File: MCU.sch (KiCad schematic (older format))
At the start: 18 parts, among them J2 JTAG, J3 BOOT, U6 STM32F303RETx

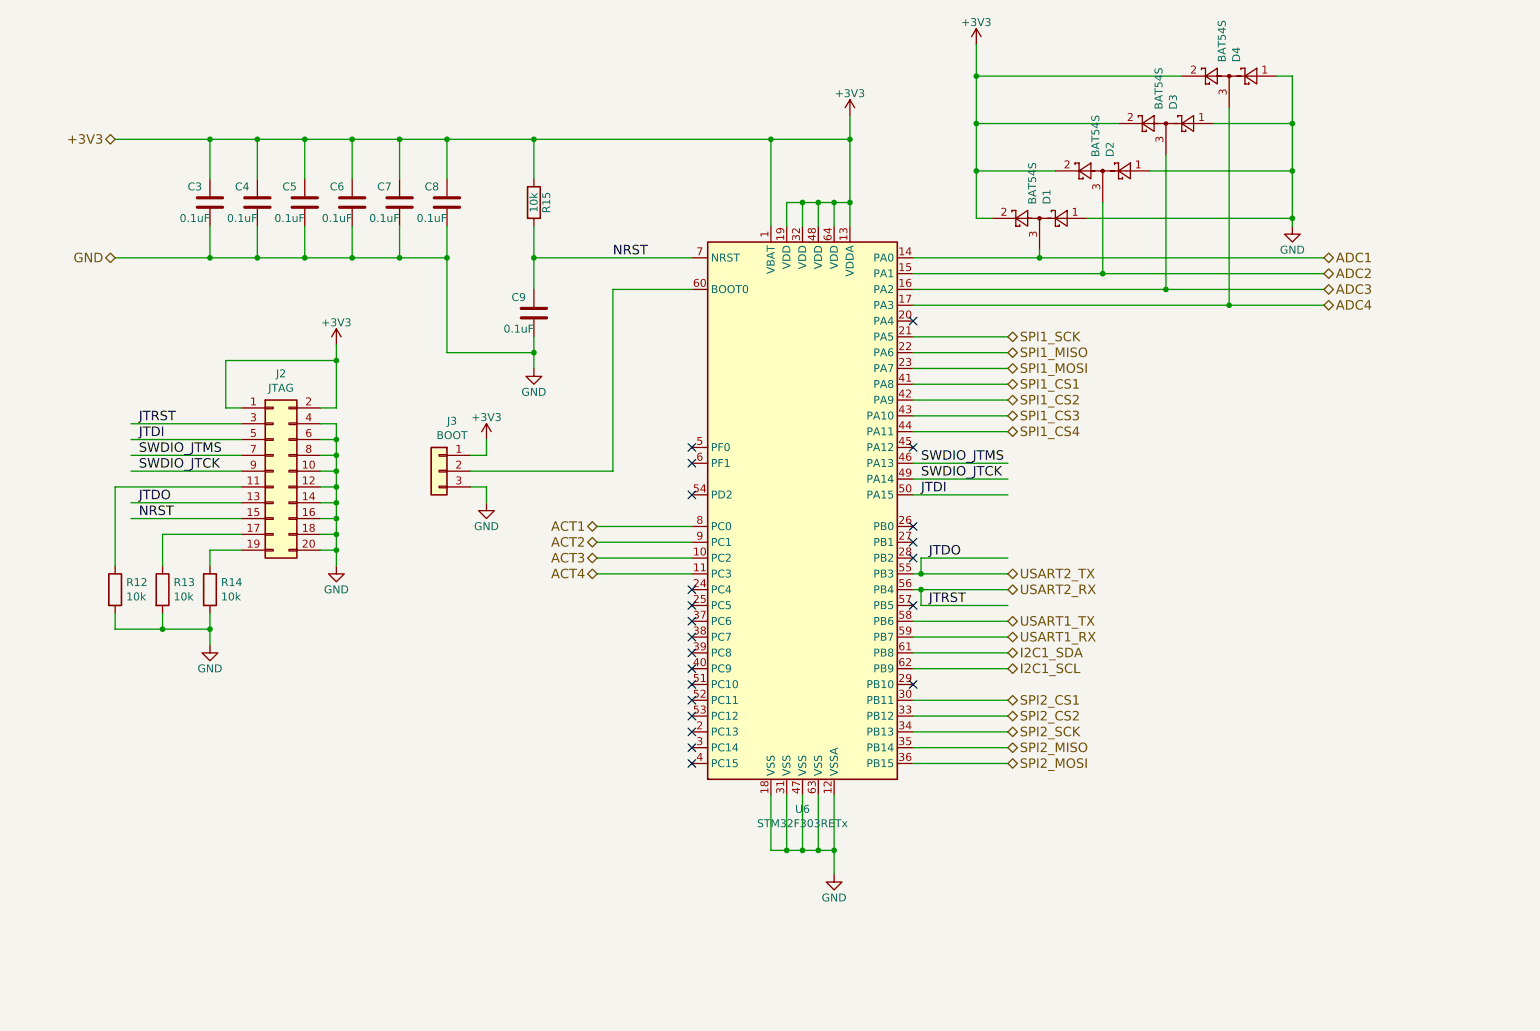
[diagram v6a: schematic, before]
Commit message: Add external oscillator Add BOOT0 pulldown Remove NRST external pullup Add test LEDs Smaller JTAG connector
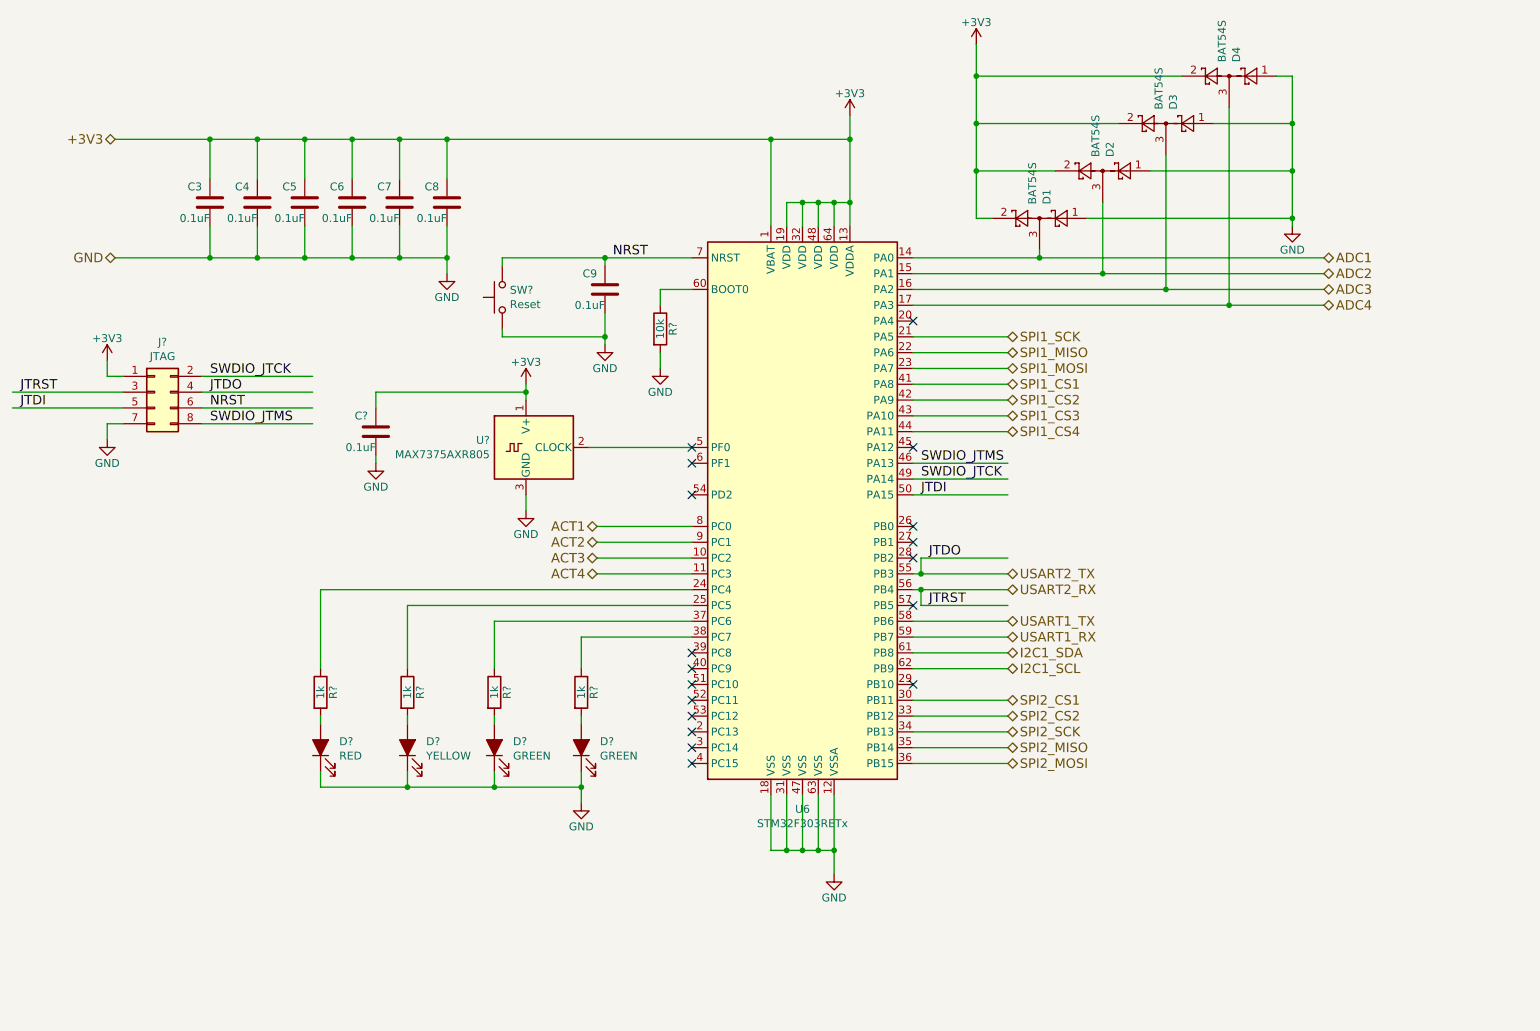
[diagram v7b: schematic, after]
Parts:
- removed J2: JTAG, Connector_PinHeader_2.54mm:PinHeader_2x10_P2.54mm_Vertical, symbol Connector_Generic:Conn_02x10_Odd_Even
- removed J3: BOOT, Connector_PinHeader_2.54mm:PinHeader_1x03_P2.54mm_Vertical, symbol Connector_Generic:Conn_01x03
- removed R12, R13, R14, R15: 10k, Resistor_SMD:R_1206_3216Metric_Pad1.42x1.75mm_HandSolder, symbol Device:R
- added C?: 0.1uF, Capacitor_SMD:C_0603_1608Metric_Pad1.05x0.95mm_HandSolder, symbol Device:C
- added D?: RED, LED_SMD:LED_0603_1608Metric_Pad1.05x0.95mm_HandSolder, symbol Device:LED_ALT
- added D?: YELLOW, LED_SMD:LED_0603_1608Metric_Pad1.05x0.95mm_HandSolder, symbol Device:LED_ALT
- added D? (x2): GREEN, LED_SMD:LED_0603_1608Metric_Pad1.05x0.95mm_HandSolder, symbol Device:LED_ALT
- added J?: JTAG, Connector_PinHeader_1.27mm:PinHeader_2x04_P1.27mm_Vertical_SMD, symbol Connector_Generic:Conn_02x04_Odd_Even
- added R?: 10k, Resistor_SMD:R_1206_3216Metric_Pad1.42x1.75mm_HandSolder, symbol Device:R
- added R? (x4): 1k, Resistor_SMD:R_1206_3216Metric_Pad1.42x1.75mm_HandSolder, symbol Device:R
- added SW?: Reset, Button_Switch_SMD:SW_Push_1P1T_NO_CK_KMR2, symbol Switch:SW_Push
- added U?: MAX7375AXR805, Package_TO_SOT_SMD:SOT-323_SC-70, symbol Oscillator:MAX7375AXR805
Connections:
- wire segments 165 -> 156
- no-connect marks 22 -> 18
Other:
- moved on the sheet: C9

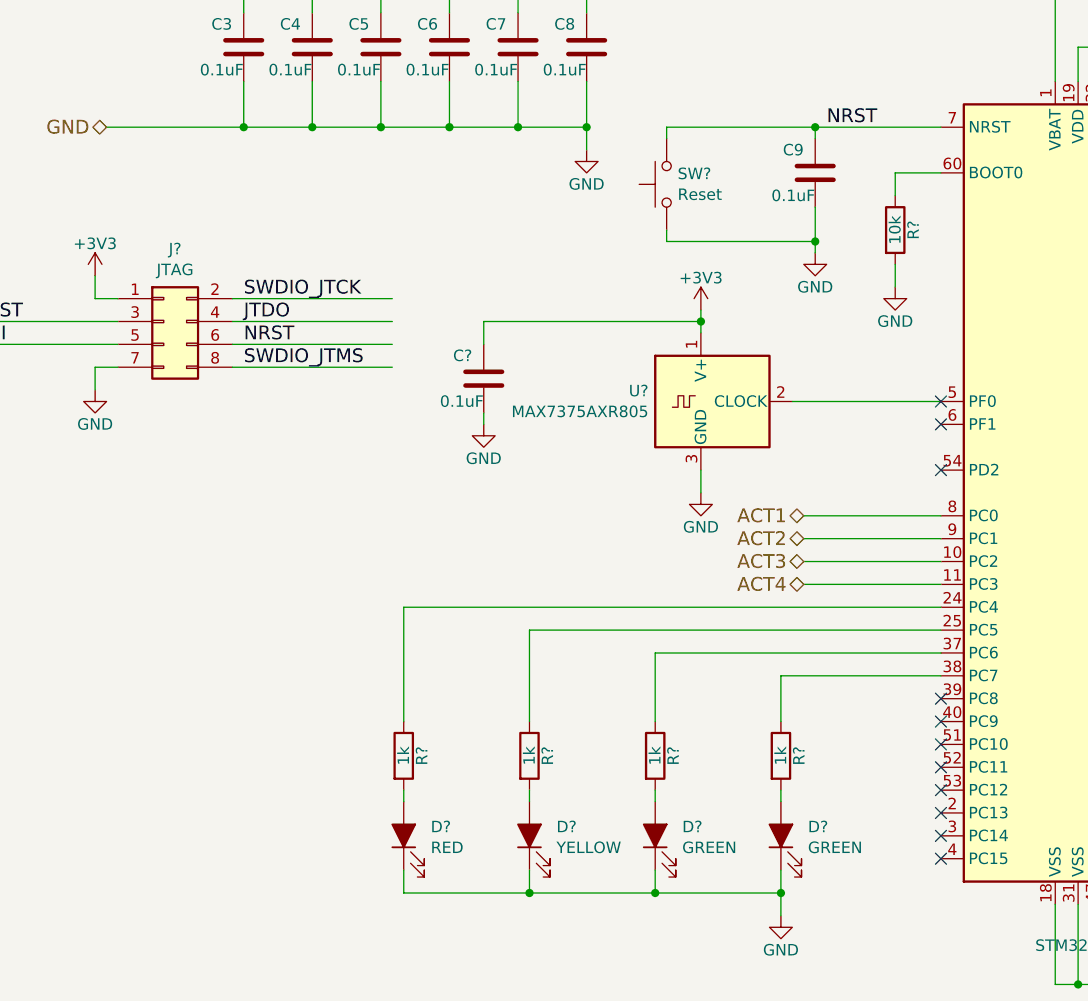
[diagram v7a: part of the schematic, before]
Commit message: Annotated schematic Added 2N7002 packages Updated PCB
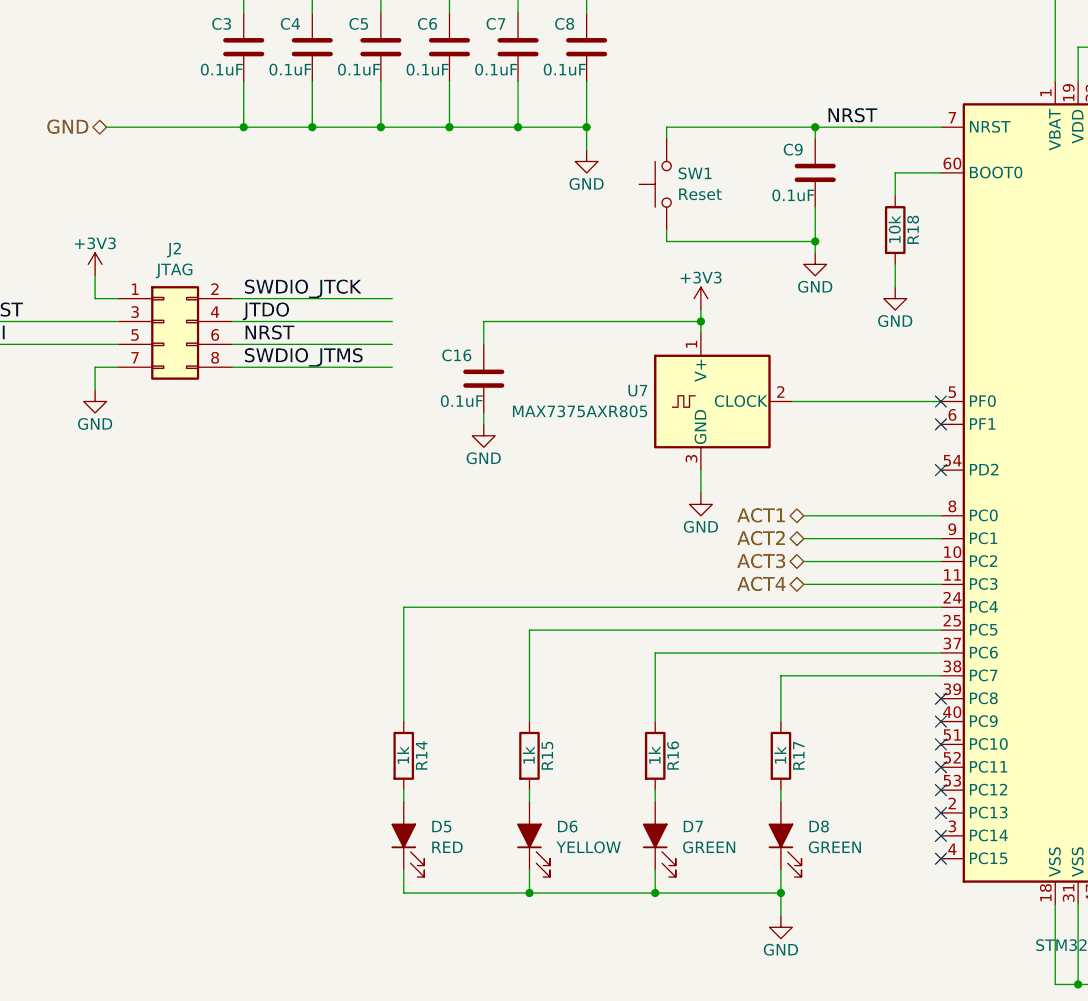
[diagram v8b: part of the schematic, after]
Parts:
- gave numbers to parts that had none: 13
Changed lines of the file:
@@
 $EndComp
 $Comp
-L Oscillator:MAX7375AXR805 U?
+L Oscillator:MAX7375AXR805 U7
 U 1 1 5E51A441
 P 3950 3650
-F 0 "U?" H 3721 3696 50  0000 R CNN
+F 0 "U7" H 3721 3696 50  0000 R CNN
 F 1 "MAX7375AXR805" H 3721 3605 50  0000 R CNN
 F 2 "Package_TO_SOT_SMD:SOT-323_SC-70" H 5050 3300 50  0001 C CNN
@@
 	4800 2650 4800 2750
 $Comp
-L power:+3V3 #PWR?
+L power:+3V3 #PWR0108
 U 1 1 5E55F7C8
 P 3950 3250
-F 0 "#PWR?" H 3950 3100 50  0001 C CNN
+F 0 "#PWR0108" H 3950 3100 50  0001 C CNN
 F 1 "+3V3" H 3950 3390 50  0000 C CNN
 F 2 "" H 3950 3250 50  0001 C CNN
@@
 $EndComp
 $Comp
-L power:GND #PWR?
+L power:GND #PWR0109
 U 1 1 5E56A1A9
 P 3950 4050
-F 0 "#PWR?" H 3950 3800 50  0001 C CNN
+F 0 "#PWR0109" H 3950 3800 50  0001 C CNN
 F 1 "GND" H 3950 3900 50  0000 C CNN
 F 2 "" H 3950 4050 50  0001 C CNN
@@
 $EndComp
 $Comp
-L Device:C C?
+L Device:C C16
 U 1 1 5E573F44
 P 3000 3550
-F 0 "C?" H 3050 3450 50  0000 L CNN
+F 0 "C16" H 3050 3450 50  0000 L CNN
 F 1 "0.1uF" H 3000 3650 50  0000 L CNN
 F 2 "Capacitor_SMD:C_0603_1608Metric_Pad1.05x0.95mm_HandSolder" H 3038 3400 50  0001 C CNN
@@
 	3950 3950 3950 4050
 $Comp
-L power:GND #PWR?
+L power:GND #PWR0110
 U 1 1 5E5CDC75
 P 3000 3750
-F 0 "#PWR?" H 3000 3500 50  0001 C CNN
+F 0 "#PWR0110" H 3000 3500 50  0001 C CNN
 F 1 "GND" H 3000 3600 50  0000 C CNN
 F 2 "" H 3000 3750 50  0001 C CNN
@@
 	3000 3700 3000 3750
 $Comp
-L Device:R R?
+L Device:R R18
 U 1 1 5E672F57
 P 4800 2900
-F 0 "R?" V 4880 2900 50  0000 C CNN
+F 0 "R18" V 4880 2900 50  0000 C CNN
 F 1 "10k" V 4800 2900 50  0000 C CNN
 F 2 "Resistor_SMD:R_1206_3216Metric_Pad1.42x1.75mm_HandSolder" V 4730 2900 50  0001 C CNN
@@
 	3450 2450 3450 2550
 $Comp
-L power:GND #PWR?
+L power:GND #PWR0111
 U 1 1 5E71C22D
 P 4450 3000
-F 0 "#PWR?" H 4450 2750 50  0001 C CNN
+F 0 "#PWR0111" H 4450 2750 50  0001 C CNN
 F 1 "GND" H 4450 2850 50  0000 C CNN
 F 2 "" H 4450 3000 50  0001 C CNN
@@
 	4450 2800 4450 2950
 $Comp
-L Switch:SW_Push SW?
+L Switch:SW_Push SW1
 U 1 1 5E76D6C7
 P 3800 2700
-F 0 "SW?" V 3846 2652 50  0000 R CNN
+F 0 "SW1" V 3846 2652 50  0000 R CNN
 F 1 "Reset" V 3755 2652 50  0000 R CNN
 F 2 "Button_Switch_SMD:SW_Push_1P1T_NO_CK_KMR2" H 3800 2900 50  0001 C CNN
@@
 	4300 4850 4300 5050
 $Comp
-L Device:R R?
+L Device:R R14
 U 1 1 5E7D0D69
 P 2650 5200
-F 0 "R?" V 2730 5200 50  0000 C CNN
+F 0 "R14" V 2730 5200 50  0000 C CNN
 F 1 "1k" V 2650 5200 50  0000 C CNN
 F 2 "Resistor_SMD:R_1206_3216Metric_Pad1.42x1.75mm_HandSolder" V 2580 5200 50  0001 C CNN
@@
 $EndComp
 $Comp
-L Device:R R?
+L Device:R R15
 U 1 1 5E7DB47A
 P 3200 5200
-F 0 "R?" V 3280 5200 50  0000 C CNN
+F 0 "R15" V 3280 5200 50  0000 C CNN
 F 1 "1k" V 3200 5200 50  0000 C CNN
 F 2 "Resistor_SMD:R_1206_3216Metric_Pad1.42x1.75mm_HandSolder" V 3130 5200 50  0001 C CNN
@@
 $EndComp
 $Comp
-L Device:R R?
+L Device:R R16
 U 1 1 5E7E47CA
 P 3750 5200
-F 0 "R?" V 3830 5200 50  0000 C CNN
+F 0 "R16" V 3830 5200 50  0000 C CNN
 F 1 "1k" V 3750 5200 50  0000 C CNN
 F 2 "Resistor_SMD:R_1206_3216Metric_Pad1.42x1.75mm_HandSolder" V 3680 5200 50  0001 C CNN
@@
 $EndComp
 $Comp
-L Device:R R?
+L Device:R R17
 U 1 1 5E7EDA7F
 P 4300 5200
-F 0 "R?" V 4380 5200 50  0000 C CNN
+F 0 "R17" V 4380 5200 50  0000 C CNN
 F 1 "1k" V 4300 5200 50  0000 C CNN
 F 2 "Resistor_SMD:R_1206_3216Metric_Pad1.42x1.75mm_HandSolder" V 4230 5200 50  0001 C CNN
@@
 $EndComp
 $Comp
-L Device:LED_ALT D?
+L Device:LED_ALT D5
 U 1 1 5E7F7CD5
 P 2650 5550
-F 0 "D?" V 2689 5432 50  0000 R CNN
+F 0 "D5" V 2689 5432 50  0000 R CNN
 F 1 "RED" V 2598 5432 50  0000 R CNN
 F 2 "LED_SMD:LED_0603_1608Metric_Pad1.05x0.95mm_HandSolder" H 2650 5550 50  0001 C CNN
@@
 $EndComp
 $Comp
-L Device:LED_ALT D?
+L Device:LED_ALT D6
 U 1 1 5E7F9DA7
 P 3200 5550
-F 0 "D?" V 3239 5432 50  0000 R CNN
+F 0 "D6" V 3239 5432 50  0000 R CNN
 F 1 "YELLOW" V 3148 5432 50  0000 R CNN
 F 2 "LED_SMD:LED_0603_1608Metric_Pad1.05x0.95mm_HandSolder" H 3200 5550 50  0001 C CNN
@@
 $EndComp
 $Comp
-L Device:LED_ALT D?
+L Device:LED_ALT D7
 U 1 1 5E8032B2
 P 3750 5550
-F 0 "D?" V 3789 5432 50  0000 R CNN
+F 0 "D7" V 3789 5432 50  0000 R CNN
 F 1 "GREEN" V 3698 5432 50  0000 R CNN
 F 2 "LED_SMD:LED_0603_1608Metric_Pad1.05x0.95mm_HandSolder" H 3750 5550 50  0001 C CNN
@@
 $EndComp
 $Comp
-L Device:LED_ALT D?
+L Device:LED_ALT D8
 U 1 1 5E80C6C7
 P 4300 5550
-F 0 "D?" V 4339 5432 50  0000 R CNN
+F 0 "D8" V 4339 5432 50  0000 R CNN
 F 1 "GREEN" V 4248 5432 50  0000 R CNN
 F 2 "LED_SMD:LED_0603_1608Metric_Pad1.05x0.95mm_HandSolder" H 4300 5550 50  0001 C CNN
@@
 	4300 5350 4300 5400
 $Comp
-L power:GND #PWR?
+L power:GND #PWR0112
 U 1 1 5E8935ED
 P 4300 5900
-F 0 "#PWR?" H 4300 5650 50  0001 C CNN
+F 0 "#PWR0112" H 4300 5650 50  0001 C CNN
 F 1 "GND" H 4300 5750 50  0000 C CNN
 F 2 "" H 4300 5900 50  0001 C CNN
@@
 Connection ~ 3200 5800
 $Comp
-L Connector_Generic:Conn_02x04_Odd_Even J?
+L Connector_Generic:Conn_02x04_Odd_Even J2
 U 1 1 5E916772
 P 1600 3300
-F 0 "J?" H 1650 3617 50  0000 C CNN
+F 0 "J2" H 1650 3617 50  0000 C CNN
 F 1 "JTAG" H 1650 3526 50  0000 C CNN
 F 2 "Connector_PinHeader_1.27mm:PinHeader_2x04_P1.27mm_Vertical_SMD" H 1600 3300 50  0001 C CNN
